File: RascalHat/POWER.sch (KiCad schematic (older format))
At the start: 11 parts, among them X1 Conn_01x02, X2 Conn_01x02, X3 Conn_01x02

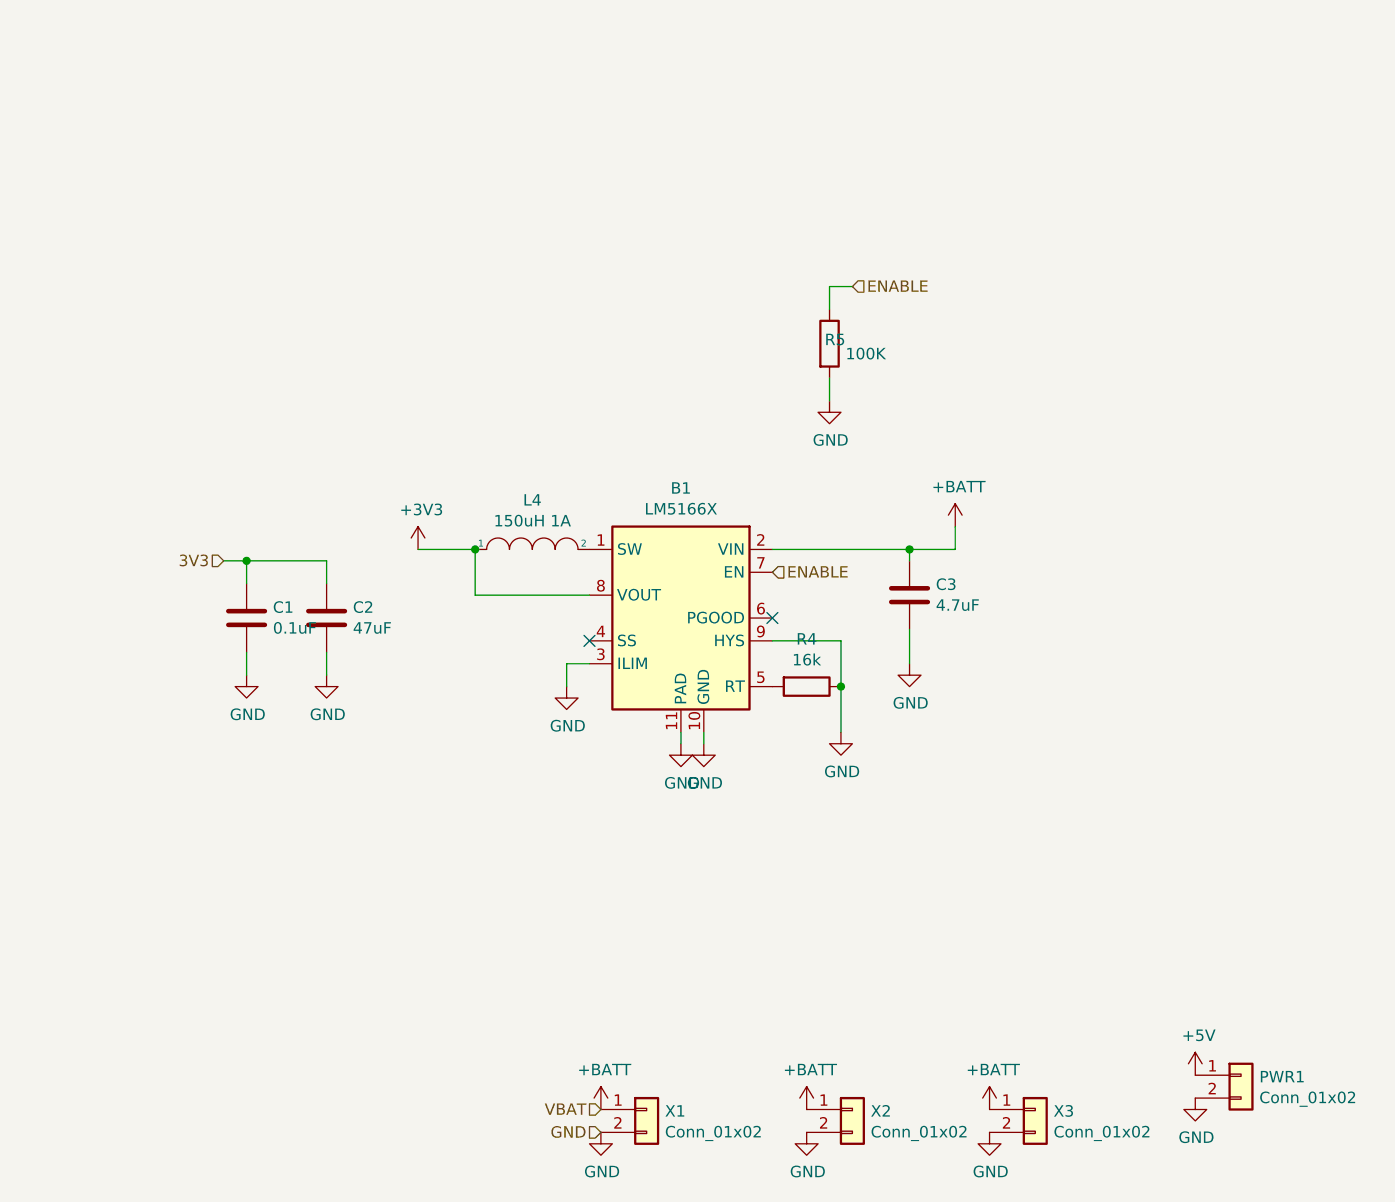
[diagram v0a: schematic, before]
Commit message: schematic done, symbol-footprint done, pcb started
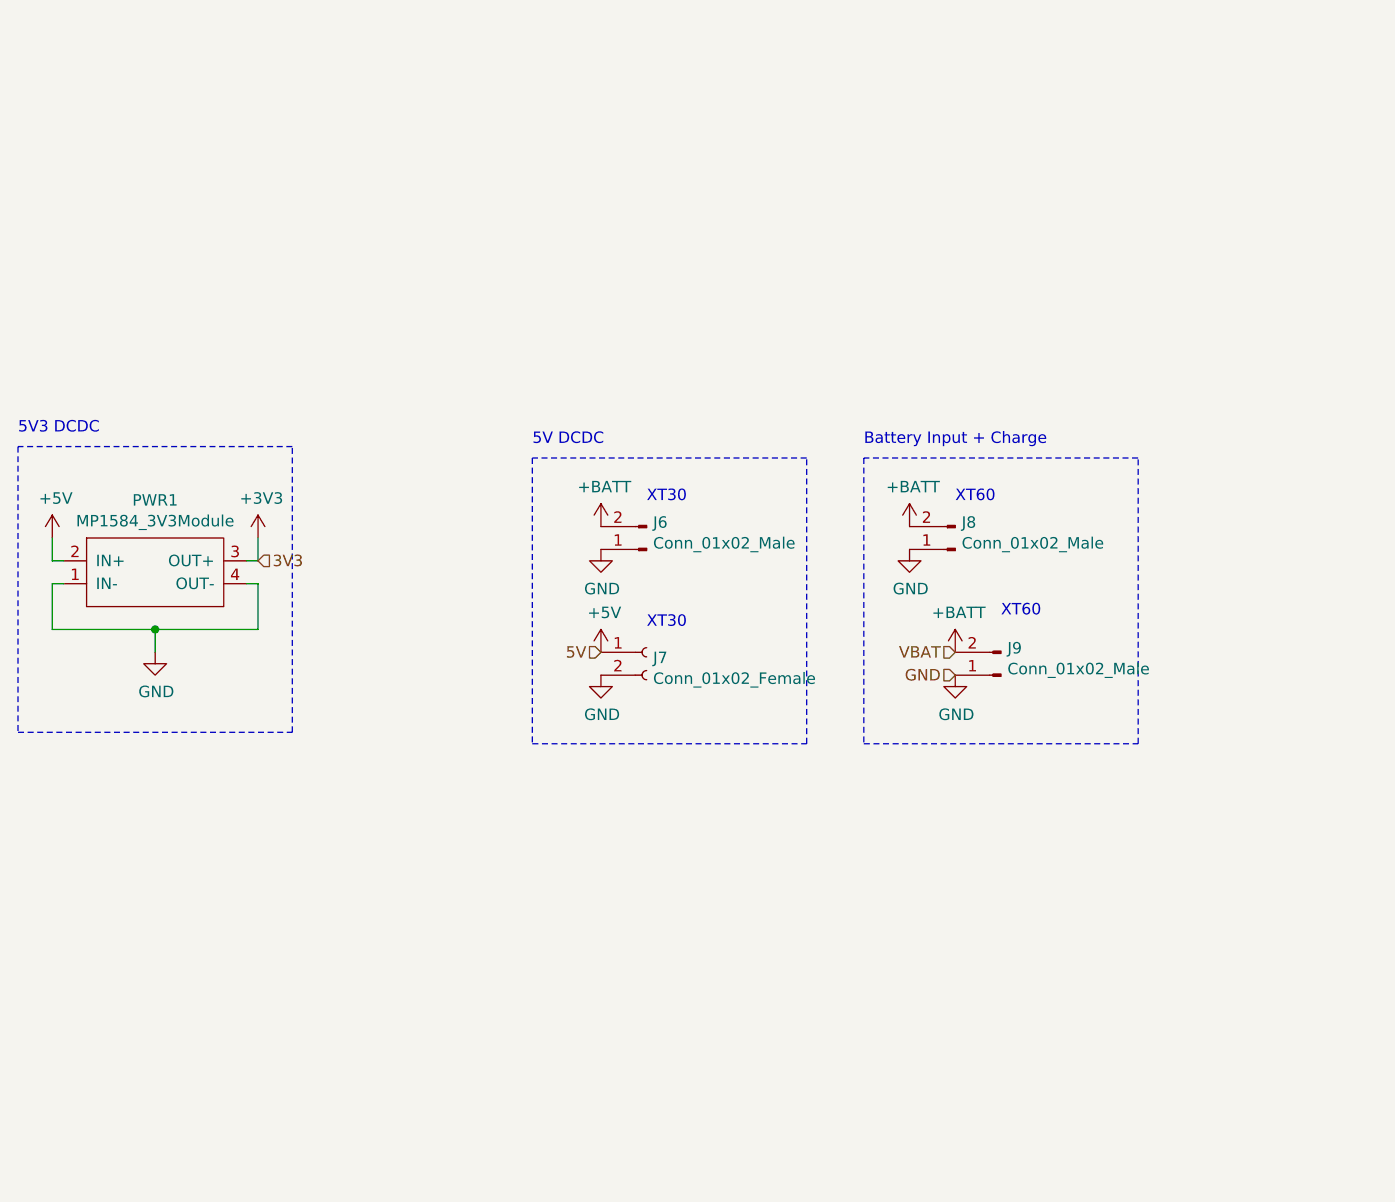
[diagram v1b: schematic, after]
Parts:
- removed B1: LM5166X, Package_SON:Texas_S-PVSON-N10_ThermalVias, symbol Regulator_Switching:LM5166X
- removed C1: 0.1uF, symbol Device:C
- removed C2: 47uF, symbol Device:C
- removed C3: 4.7uF, symbol Device:C
- removed L4: 150uH 1A, symbol pspice:INDUCTOR
- removed PWR1, X1, X2, X3: Conn_01x02, symbol Connector_Generic:Conn_01x02
- removed R4: 16k, symbol Device:R
- removed R5: 100K, symbol Device:R
- added J6: Conn_01x02_Male, Connector_AMASS:AMASS_XT30U-M_1x02_P5.0mm_Vertical, symbol Connector:Conn_01x02_Male
- added J7: Conn_01x02_Female, Connector_AMASS:AMASS_XT30U-F_1x02_P5.0mm_Vertical, symbol Connector:Conn_01x02_Female
- added J8, J9: Conn_01x02_Male, RascalHat:XT60-M, symbol Connector:Conn_01x02_Male
- added PWR1: MP1584_3V3Module, RascalHat:MP1584-Jacobs-Parts-Module, symbol Rascal_KiCAD_LIB:MP1584_3V3Module
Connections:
- net +3V3: now also PWR1.3 (OUT+)
- net +5V: now also J7.1 (Pin_1), PWR1.2 (IN+)
- net +BATT: now also J6.2 (Pin_2), J8.2 (Pin_2), J9.2 (Pin_2)
- net GND: now also J6.1 (Pin_1), J7.2 (Pin_2), J8.1 (Pin_1), J9.1 (Pin_1), PWR1.1 (IN-), PWR1.4 (OUT-)
- no-connect marks 2 -> 0
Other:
- note added: "5V DCDC"
- note added: "5V3 DCDC"
- note added: "Battery Input + Charge"
- note added: "XT30"
- note added: "XT60"

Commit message: schematic updated, all footprints created, pcb layout started
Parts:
- added C5: CP1, Capacitor_SMD:CP_Elec_4x4.5, symbol Device:CP1
- added D2, D3, D4: LED, Diode_SMD:D_0805_2012Metric, symbol Device:LED
- added R10: 3k3, Resistor_SMD:R_0805_2012Metric, symbol Device:R
- added R8: 470, Resistor_SMD:R_0805_2012Metric, symbol Device:R
- added R9: 2k2, Resistor_SMD:R_0805_2012Metric, symbol Device:R
- J6: footprint Connector_AMASS:AMASS_XT30U-M_1x02_P5.0mm_Vertical -> RascalHat:XT30U-M-Horizontal
- J7: footprint Connector_AMASS:AMASS_XT30U-F_1x02_P5.0mm_Vertical -> RascalHat:XT30U-F-Horizontal
- J8: footprint RascalHat:XT60-M -> RascalHat:XT60-M-Horizontal
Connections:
- net +3V3: now also C5.1, R8.1
- net +5V: now also R9.1
- net +BATT: now also R10.1
- net GND: now also C5.2, D2.1 (K), D3.1 (K), D4.1 (K)
- new net: D2.2 (A), R8.2
- new net: D3.2 (A), R9.2
- new net: D4.2 (A), R10.2
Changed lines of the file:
@@
 F 0 "J8" H 6672 3182 50  0000 R CNN
 F 1 "Conn_01x02_Male" H 6672 3273 50  0000 R CNN
-F 2 "RascalHat:XT60-M" H 6700 3300 50  0001 C CNN
+F 2 "RascalHat:XT60-M-Horizontal" H 6700 3300 50  0001 C CNN
 F 3 "~" H 6700 3300 50  0001 C CNN
 	1    6700 3300
@@
 F 0 "J7" H 5378 3726 50  0000 L CNN
 F 1 "Conn_01x02_Female" H 5378 3635 50  0000 L CNN
-F 2 "Connector_AMASS:AMASS_XT30U-F_1x02_P5.0mm_Vertical" H 5350 3750 50  0001 C CNN
+F 2 "RascalHat:XT30U-F-Horizontal" H 5350 3750 50  0001 C CNN
 F 3 "~" H 5350 3750 50  0001 C CNN
 	1    5350 3750
@@
 F 0 "J6" H 5322 3182 50  0000 R CNN
 F 1 "Conn_01x02_Male" H 5322 3273 50  0000 R CNN
-F 2 "Connector_AMASS:AMASS_XT30U-M_1x02_P5.0mm_Vertical" H 5350 3300 50  0001 C CNN
+F 2 "RascalHat:XT30U-M-Horizontal" H 5350 3300 50  0001 C CNN
 F 3 "~" H 5350 3300 50  0001 C CNN
 	1    5350 3300
@@
 Text Notes 5350 3100 0    50   ~ 0
 XT30
-$Comp
-L Connector:Conn_01x02_Male J9
-U 1 1 619F7430
-P 6900 3850
-F 0 "J9" H 6872 3732 50  0000 R CNN
-F 1 "Conn_01x02_Male" H 6872 3823 50  0000 R CNN
-F 2 "RascalHat:XT60-M" H 6900 3850 50  0001 C CNN
-F 3 "~" H 6900 3850 50  0001 C CNN
-	1    6900 3850
-	-1   0    0    1
-$EndComp
 Wire Notes Line
 	2600 2850 2600 4100
@@
 Text HLabel 3650 3350 2    50   Input ~ 0
 3V3
+$Comp
+L Device:LED D?
+U 1 1 61D39612
+P 3350 1850
+AR Path="/61D39612" Ref="D?"  Part="1"
+AR Path="/61887FF8/61D39612" Ref="D2"  Part="1"
+F 0 "D2" V 3389 1733 50  0000 R CNN
+F 1 "LED" V 3298 1733 50  0000 R CNN
+F 2 "Diode_SMD:D_0805_2012Metric" H 3350 1850 50  0001 C CNN
+F 3 "~" H 3350 1850 50  0001 C CNN
+	1    3350 1850
+	0    -1   -1   0
+$EndComp
+$Comp
+L Device:R R8
+U 1 1 61D39980
+P 3350 1450
+F 0 "R8" H 3420 1496 50  0000 L CNN
+F 1 "470" H 3420 1405 50  0000 L CNN
+F 2 "Resistor_SMD:R_0805_2012Metric" V 3280 1450 50  0001 C CNN
+F 3 "~" H 3350 1450 50  0001 C CNN
+	1    3350 1450
+	1    0    0    -1
+$EndComp
+$Comp
+L power:+3V3 #PWR0108
+U 1 1 61D39D1E
+P 3350 1200
+F 0 "#PWR0108" H 3350 1050 50  0001 C CNN
+F 1 "+3V3" H 3365 1373 50  0000 C CNN
+F 2 "" H 3350 1200 50  0001 C CNN
+F 3 "" H 3350 1200 50  0001 C CNN
+	1    3350 1200
+	1    0    0    -1
+$EndComp
+Wire Wire Line
+	3350 1200 3350 1300
+Wire Wire Line
+	3350 1600 3350 1700
+$Comp
+L power:GND #PWR?
+U 1 1 61D3D5A2
+P 3350 2100
+AR Path="/61D3D5A2" Ref="#PWR?"  Part="1"
+AR Path="/61887FF8/61D3D5A2" Ref="#PWR0109"  Part="1"
+F 0 "#PWR0109" H 3350 1850 50  0001 C CNN
+F 1 "GND" H 3355 1927 50  0000 C CNN
+F 2 "" H 3350 2100 50  0001 C CNN
+F 3 "" H 3350 2100 50  0001 C CNN
+	1    3350 2100
+	1    0    0    -1
+$EndComp
+Wire Wire Line
+	3350 2100 3350 2000
+$Comp
+L Device:LED D?
+U 1 1 61D3F574
+P 3750 1850
+AR Path="/61D3F574" Ref="D?"  Part="1"
+AR Path="/61887FF8/61D3F574" Ref="D3"  Part="1"
+F 0 "D3" V 3789 1733 50  0000 R CNN
+F 1 "LED" V 3698 1733 50  0000 R CNN
+F 2 "Diode_SMD:D_0805_2012Metric" H 3750 1850 50  0001 C CNN
+F 3 "~" H 3750 1850 50  0001 C CNN
+	1    3750 1850
+	0    -1   -1   0
+$EndComp
+$Comp
+L Device:R R9
+U 1 1 61D3F57A
+P 3750 1450
+F 0 "R9" H 3820 1496 50  0000 L CNN
+F 1 "2k2" H 3820 1405 50  0000 L CNN
+F 2 "Resistor_SMD:R_0805_2012Metric" V 3680 1450 50  0001 C CNN
+F 3 "~" H 3750 1450 50  0001 C CNN
+	1    3750 1450
+	1    0    0    -1
+$EndComp
+Wire Wire Line
+	3750 1200 3750 1300
+Wire Wire Line
+	3750 1600 3750 1700
+$Comp
+L power:GND #PWR?
+U 1 1 61D3F588
+P 3750 2100
+AR Path="/61D3F588" Ref="#PWR?"  Part="1"
+AR Path="/61887FF8/61D3F588" Ref="#PWR0110"  Part="1"
+F 0 "#PWR0110" H 3750 1850 50  0001 C CNN
+F 1 "GND" H 3755 1927 50  0000 C CNN
+F 2 "" H 3750 2100 50  0001 C CNN
+F 3 "" H 3750 2100 50  0001 C CNN
+	1    3750 2100
+	1    0    0    -1
+$EndComp
+Wire Wire Line
+	3750 2100 3750 2000
+$Comp
+L power:+5V #PWR?
+U 1 1 61D3F94A
+P 3750 1200
+AR Path="/61D3F94A" Ref="#PWR?"  Part="1"
+AR Path="/61887FF8/61D3F94A" Ref="#PWR0111"  Part="1"
+F 0 "#PWR0111" H 3750 1050 50  0001 C CNN
+F 1 "+5V" H 3765 1373 50  0000 C CNN
+F 2 "" H 3750 1200 50  0001 C CNN
+F 3 "" H 3750 1200 50  0001 C CNN
+	1    3750 1200
+	1    0    0    -1
+$EndComp
+$Comp
+L Device:LED D?
+U 1 1 61D4277A
+P 4150 1850
+AR Path="/61D4277A" Ref="D?"  Part="1"
+AR Path="/61887FF8/61D4277A" Ref="D4"  Part="1"
+F 0 "D4" V 4189 1733 50  0000 R CNN
+F 1 "LED" V 4098 1733 50  0000 R CNN
+F 2 "Diode_SMD:D_0805_2012Metric" H 4150 1850 50  0001 C CNN
+F 3 "~" H 4150 1850 50  0001 C CNN
+	1    4150 1850
+	0    -1   -1   0
+$EndComp
+$Comp
+L Device:R R10
+U 1 1 61D42780
+P 4150 1450
+F 0 "R10" H 4220 1496 50  0000 L CNN
+F 1 "3k3" H 4220 1405 50  0000 L CNN
+F 2 "Resistor_SMD:R_0805_2012Metric" V 4080 1450 50  0001 C CNN
+F 3 "~" H 4150 1450 50  0001 C CNN
+	1    4150 1450
+	1    0    0    -1
+$EndComp
+Wire Wire Line
+	4150 1200 4150 1300
+Wire Wire Line
+	4150 1600 4150 1700
+$Comp
+L power:GND #PWR?
+U 1 1 61D42788
+P 4150 2100
+AR Path="/61D42788" Ref="#PWR?"  Part="1"
+AR Path="/61887FF8/61D42788" Ref="#PWR0112"  Part="1"
+F 0 "#PWR0112" H 4150 1850 50  0001 C CNN
+F 1 "GND" H 4155 1927 50  0000 C CNN
+F 2 "" H 4150 2100 50  0001 C CNN
+F 3 "" H 4150 2100 50  0001 C CNN
+	1    4150 2100
+	1    0    0    -1
+$EndComp
+Wire Wire Line
+	4150 2100 4150 2000
+$Comp
+L power:+BATT #PWR?
+U 1 1 61D42AC2
+P 4150 1200
+AR Path="/61D42AC2" Ref="#PWR?"  Part="1"
+AR Path="/61887FF8/61D42AC2" Ref="#PWR0113"  Part="1"
+F 0 "#PWR0113" H 4150 1050 50  0001 C CNN
+F 1 "+BATT" H 4165 1373 50  0000 C CNN
+F 2 "" H 4150 1200 50  0001 C CNN
+F 3 "" H 4150 1200 50  0001 C CNN
+	1    4150 1200
+	1    0    0    -1
+$EndComp
+$Comp
+L Device:CP1 C5
+U 1 1 61D45811
+P 4100 3600
+F 0 "C5" H 4215 3646 50  0000 L CNN
+F 1 "CP1" H 4215 3555 50  0000 L CNN
+F 2 "Capacitor_SMD:CP_Elec_4x4.5" H 4100 3600 50  0001 C CNN
+F 3 "~" H 4100 3600 50  0001 C CNN
+	1    4100 3600
+	1    0    0    -1
+$EndComp
+$Comp
+L power:+3V3 #PWR0114
+U 1 1 61D45B95
+P 4100 3350
+F 0 "#PWR0114" H 4100 3200 50  0001 C CNN
+F 1 "+3V3" H 4115 3523 50  0000 C CNN
+F 2 "" H 4100 3350 50  0001 C CNN
+F 3 "" H 4100 3350 50  0001 C CNN
+	1    4100 3350
+	1    0    0    -1
+$EndComp
+Wire Wire Line
+	4100 3350 4100 3450
+$Comp
+L power:GND #PWR?
+U 1 1 61D46385
+P 4100 3850
+AR Path="/61D46385" Ref="#PWR?"  Part="1"
+AR Path="/61887FF8/61D46385" Ref="#PWR0115"  Part="1"
+F 0 "#PWR0115" H 4100 3600 50  0001 C CNN
+F 1 "GND" H 4105 3677 50  0000 C CNN
+F 2 "" H 4100 3850 50  0001 C CNN
+F 3 "" H 4100 3850 50  0001 C CNN
+	1    4100 3850
+	1    0    0    -1
+$EndComp
+Wire Wire Line
+	4100 3850 4100 3750
+$Comp
+L Connector:Conn_01x02_Male J9
+U 1 1 619F7430
+P 6900 3850
+F 0 "J9" H 6872 3732 50  0000 R CNN
+F 1 "Conn_01x02_Male" H 6872 3823 50  0000 R CNN
+F 2 "RascalHat:XT60-M" H 6900 3850 50  0001 C CNN
+F 3 "~" H 6900 3850 50  0001 C CNN
+	1    6900 3850
+	-1   0    0    1
+$EndComp
 $EndSCHEMATC
